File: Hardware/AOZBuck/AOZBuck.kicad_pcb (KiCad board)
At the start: 2 copper layers, 30 x 16 mm, 10 parts, among them J1 Conn_01x02, J2 Conn_01x02, U1 AOZ1280CI

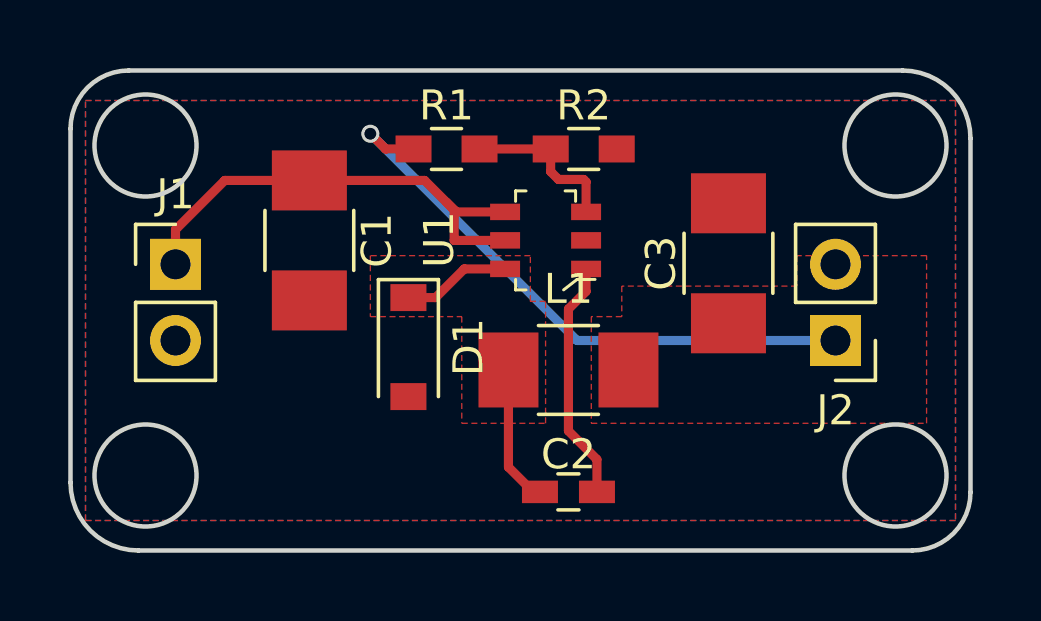
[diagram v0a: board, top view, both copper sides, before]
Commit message: Updated Buck layout.
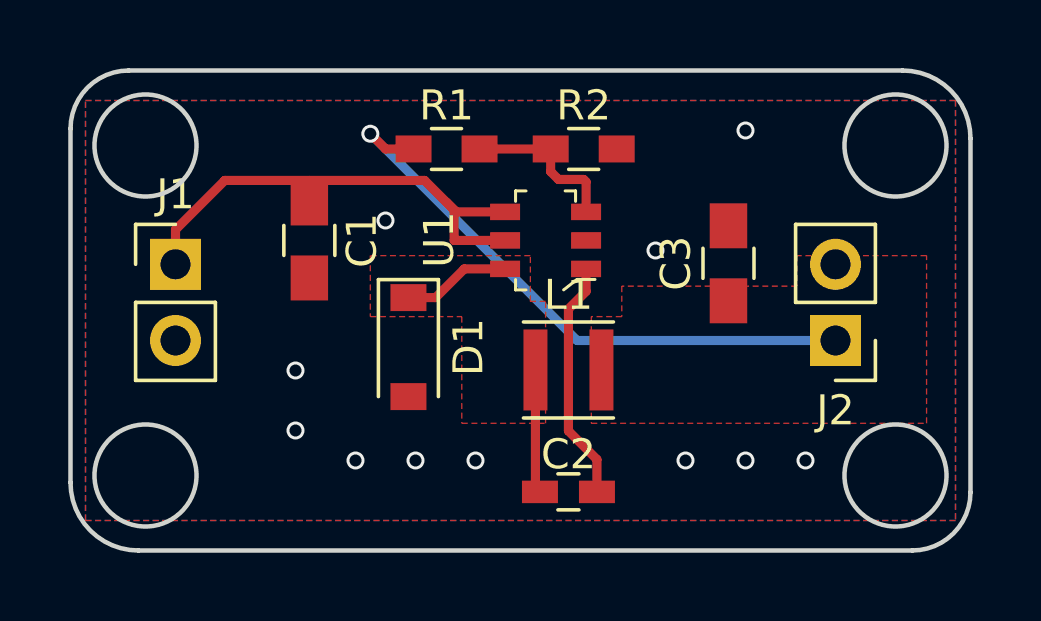
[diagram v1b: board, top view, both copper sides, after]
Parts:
- C1, C3: footprint Capacitors_SMD:C_1210_HandSoldering -> Capacitors_SMD:C_0805_HandSoldering
- L1: footprint Inductors_SMD:L_1210_HandSoldering -> Inductors_SMD:L_Taiyo-Yuden_MD-3030
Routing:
- net GND: vias 0 -> 11

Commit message: Created a small buck and LDO board.
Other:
- board text added: "AOZ1280 Buck Rev A"
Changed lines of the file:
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@@
   (general
     (thickness 1.6)
-    (drawings 12)
+    (drawings 13)
     (tracks 43)
     (zones 0)
@@
   )
   (setup
-    (last_trace_width 0.3048)
+    (last_trace_width 0.25)
     (user_trace_width 0.3048)
     (trace_clearance 0.2)
@@
     )
   )
+  (gr_text "AOZ1280 Buck Rev A" (at 147 108) (layer B.SilkS)
+    (effects (font (size 1.5 1.5) (thickness 0.3)) (justify mirror))
+  )
   (gr_line (start 134.442742 100) (end 160.237258 100) (angle 90) (layer Edge.Cuts) (width 0.15))

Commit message: Add some silkscreen items
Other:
- board text added: "12V"
- board text added: "5V"
- board text added: "GND"
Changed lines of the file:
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@@
   (general
     (thickness 1.6)
-    (drawings 13)
+    (drawings 17)
     (tracks 43)
     (zones 0)
@@
     )
   )
+  (gr_text 5V (at 161 109.5 90) (layer F.SilkS)
+    (effects (font (size 1 1) (thickness 0.25)))
+  )
+  (gr_text GND (at 161 106 90) (layer F.SilkS)
+    (effects (font (size 1 1) (thickness 0.25)))
+  )
+  (gr_text GND (at 133.5 109.5 90) (layer F.SilkS)
+    (effects (font (size 1 1) (thickness 0.25)))
+  )
+  (gr_text 12V (at 133.5 106 90) (layer F.SilkS)
+    (effects (font (size 1 1) (thickness 0.25)))
+  )
   (gr_text "AOZ1280 Buck Rev A" (at 147 108) (layer B.SilkS)

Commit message: More updates before ordering.
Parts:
- moved J1 1.50 mm to (137.5, 106.5)
- moved J2 1.25 mm to (156.8, 109.0)
- moved C3 1.18 mm to (153.2, 106.4)
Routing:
- net Net-(C1-Pad1): track 16.3 -> 14.5 mm
- net Net-(C3-Pad1): track 20.0 -> 18.8 mm
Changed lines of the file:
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@@
   (general
     (thickness 1.6)
-    (drawings 17)
-    (tracks 43)
+    (drawings 21)
+    (tracks 44)
     (zones 0)
     (modules 10)
@@
   )
   (setup
-    (last_trace_width 0.25)
+    (last_trace_width 0.3048)
     (user_trace_width 0.3048)
     (trace_clearance 0.2)
@@
   )
   (module Pin_Headers:Pin_Header_Straight_1x02_Pitch2.54mm (layer F.Cu)
-    (at 136 106.46)
+    (at 137.5 106.5)
     (descr "Through hole straight pin header, 1x02, 2.54mm pitch, single row")
     (tags "Through hole pin header THT 1x02 2.54mm single row")
@@
   )
   (module Pin_Headers:Pin_Header_Straight_1x02_Pitch2.54mm (layer F.Cu)
-    (at 158 109 180)
+    (at 156.75 109 180)
     (descr "Through hole straight pin header, 1x02, 2.54mm pitch, single row")
     (tags "Through hole pin header THT 1x02 2.54mm single row")
@@
   )
   (module Capacitors_SMD:C_0805_HandSoldering (layer F.Cu)
-    (at 154.432 106.426 90)
+    (at 153.25 106.426 90)
     (descr "Capacitor SMD 0805, hand soldering")
     (tags "capacitor 0805")
@@
     )
   )
+  (gr_circle (center 160 113.5) (end 162.75 113.25) (layer F.SilkS) (width 0.2))
+  (gr_circle (center 160 102.5) (end 162.75 102.5) (layer F.SilkS) (width 0.2))
+  (gr_circle (center 135 113.5) (end 137.75 113.5) (layer F.SilkS) (width 0.2))
+  (gr_circle (center 135 102.5) (end 137.75 102.5) (layer F.SilkS) (width 0.2))
   (gr_text 5V (at 161 109.5 90) (layer F.SilkS)
     (effects (font (size 1 1) (thickness 0.25)))
@@
   (gr_arc (start 160.557258 114.057258) (end 160.557258 116) (angle -90) (layer Edge.Cuts) (width 0.15))
   (gr_arc (start 134.442742 101.942742) (end 134.442742 100) (angle -90) (layer Edge.Cuts) (width 0.15))
-  (segment (start 140.462 103.664) (end 137.6412 103.664) (width 0.3048) (layer F.Cu) (net 1))
-  (segment (start 137.6412 103.664) (end 136 105.3052) (width 0.3048) (layer F.Cu) (net 1))
-  (segment (start 136 105.3052) (end 136 106.46) (width 0.3048) (layer F.Cu) (net 1))
+  (segment (start 137.5 106.5) (end 137.5 105.3452) (width 0.3048) (layer F.Cu) (net 1))
+  (segment (start 137.5 105.3452) (end 138.4312 104.414) (width 0.3048) (layer F.Cu) (net 1))
+  (segment (start 138.4312 104.414) (end 139.5322 104.414) (width 0.3048) (layer F.Cu) (net 1))
+  (segment (start 139.5322 104.414) (end 140.462 104.414) (width 0.3048) (layer F.Cu) (net 1))
   (segment (start 144.304 103.664) (end 145.034 104.394) (width 0.3048) (layer F.Cu) (net 1))
   (segment (start 145.034 104.394) (end 145.354 104.714) (width 0.3048) (layer F.Cu) (net 1))
@@
   (segment (start 150.048 112.964) (end 149.098 112.014) (width 0.3048) (layer F.Cu) (net 4))
   (segment (start 150.048 114.046) (end 150.048 112.964) (width 0.3048) (layer F.Cu) (net 4))
-  (segment (start 158 109) (end 149.386 109) (width 0.3048) (layer B.Cu) (net 5))
+  (segment (start 156.75 109) (end 149.386 109) (width 0.3048) (layer B.Cu) (net 5))
   (segment (start 149.386 109) (end 142.494 102.108) (width 0.3048) (layer B.Cu) (net 5))
   (segment (start 143.934 102.616) (end 143.002 102.616) (width 0.3048) (layer F.Cu) (net 5))
